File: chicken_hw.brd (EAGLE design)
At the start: 25.7 x 38.1 mm, 19 parts, among them U2 CD74HC4051PWR

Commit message: Fix ERC errors w/ V0.3 board  VCC and S2 not connected (unrouted)
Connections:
- removed net VCC: U2.16
- net 3.3V: now also U2.16
- net N$1: now also U2.9
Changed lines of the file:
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@@
 <wire x1="19.0618" y1="22.4926" x2="20.0152" y2="21.5392" width="0.254" layer="1"/>
 <wire x1="22.86" y1="13.97" x2="20.0152" y2="13.97" width="0.254" layer="1"/>
+<contactref element="U2" pad="16"/>
+<wire x1="17.2466" y1="22.4926" x2="10.5156" y2="26.4414" width="0" layer="19" extent="1-1"/>
 </signal>
 <signal name="EN_MUX">
@@
 <signal name="N$1">
 <contactref element="R1" pad="2"/>
+<contactref element="U2" pad="9"/>
+<wire x1="8.89" y1="16.1535" x2="15.0876" y2="26.4414" width="0" layer="19" extent="1-1"/>
 </signal>
 <signal name="N$8">
@@
 <wire x1="4.445" y1="24.13" x2="4.7752" y2="23.7998" width="0.254" layer="1"/>
 </signal>
-<signal name="VCC">
-<contactref element="U2" pad="16"/>
-</signal>
 <signal name="N$2">

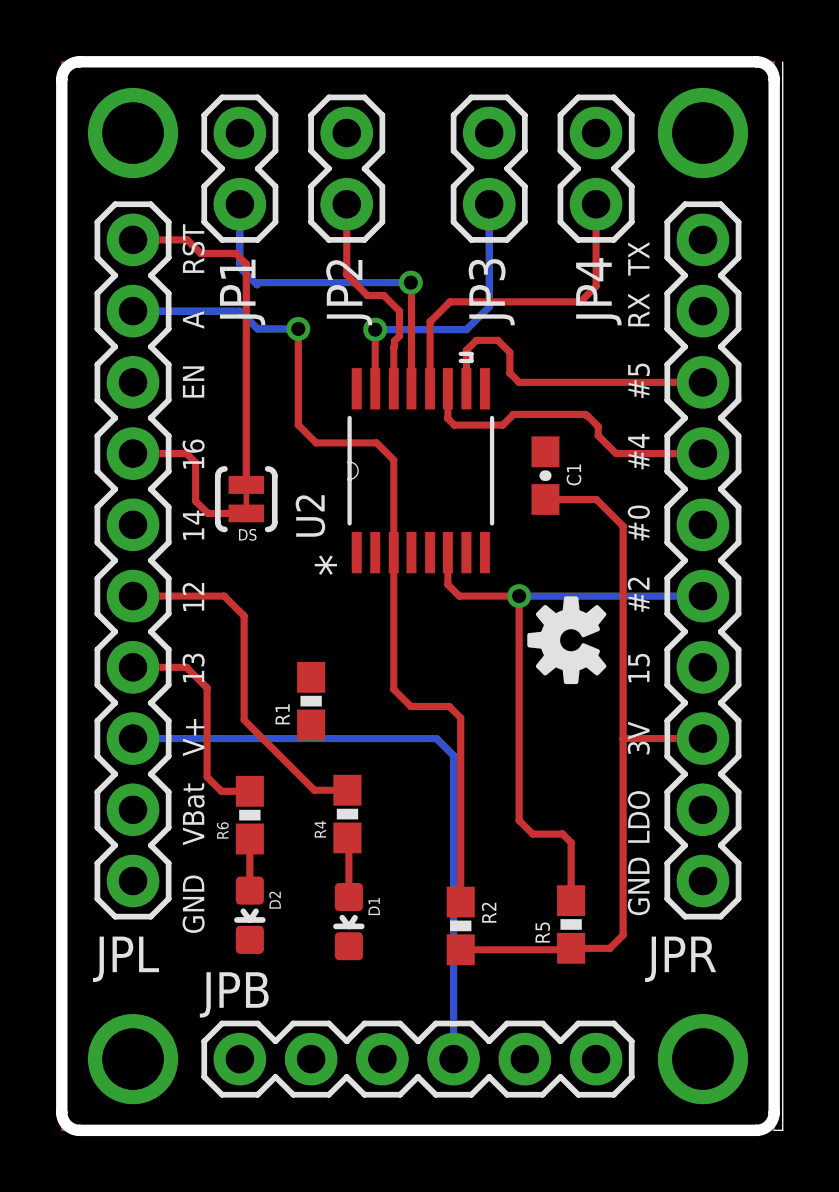
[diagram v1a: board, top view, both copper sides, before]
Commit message: Route missing signals for mux from 12c953b27b064bb54cf89404
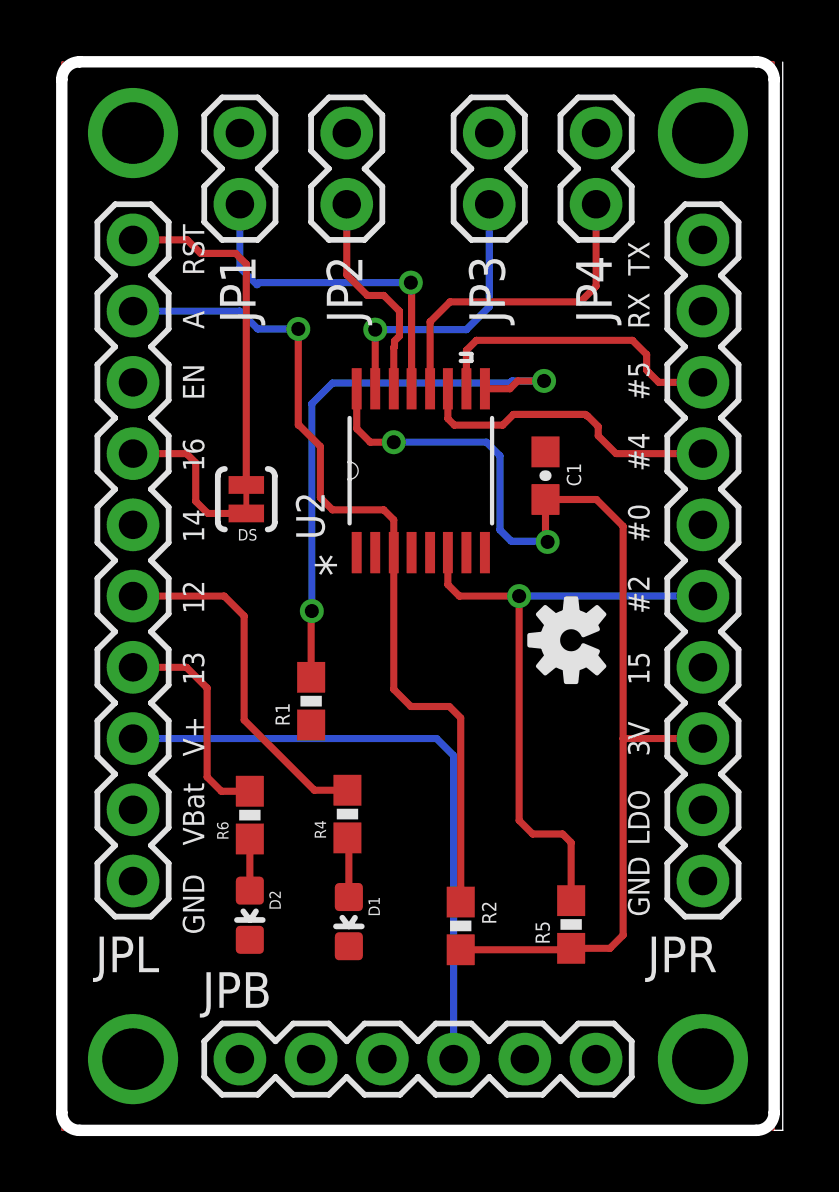
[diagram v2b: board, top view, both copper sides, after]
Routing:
- net N$1: track 0.00 -> 20.6 mm, vias 0 -> 2
- net 3.3V: track 26.6 -> 39.6 mm, vias 0 -> 2
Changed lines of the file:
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@@
 <contactref element="R2" pad="1"/>
 <contactref element="U2" pad="3"/>
-<wire x1="11.8364" y1="20.5994" x2="11.8364" y2="23.9014" width="0.254" layer="1"/>
-<wire x1="11.8364" y1="23.9014" x2="11.2268" y2="24.511" width="0.254" layer="1"/>
-<wire x1="11.2268" y1="24.511" x2="9.0678" y2="24.511" width="0.254" layer="1"/>
-<wire x1="9.0678" y1="24.511" x2="8.4328" y2="25.146" width="0.254" layer="1"/>
 <via x="8.4328" y="28.575" extent="1-16" drill="0.5" diameter="0.254"/>
 <wire x1="8.4328" y1="28.575" x2="8.4328" y2="25.146" width="0.254" layer="1"/>
@@
 <wire x1="11.8364" y1="20.5994" x2="11.8364" y2="15.7226" width="0.254" layer="1"/>
 <wire x1="11.8364" y1="15.7226" x2="12.446" y2="15.113" width="0.254" layer="1"/>
+<wire x1="8.4328" y1="25.146" x2="8.4582" y2="25.146" width="0.254" layer="1"/>
+<wire x1="8.4582" y1="25.146" x2="9.2202" y2="24.384" width="0.254" layer="1"/>
+<wire x1="9.2202" y1="24.384" x2="9.2202" y2="22.5552" width="0.254" layer="1"/>
+<wire x1="9.2202" y1="22.5552" x2="9.652" y2="22.1234" width="0.254" layer="1"/>
+<wire x1="9.652" y1="22.1234" x2="11.4808" y2="22.1234" width="0.254" layer="1"/>
+<wire x1="11.8364" y1="20.5994" x2="11.8364" y2="21.7678" width="0.254" layer="1"/>
+<wire x1="11.8364" y1="21.7678" x2="11.4808" y2="22.1234" width="0.254" layer="1"/>
 </signal>
 <signal name="EN">
@@
 <wire x1="14.4272" y1="26.4414" x2="14.4272" y2="27.813" width="0.254" layer="1"/>
 <wire x1="14.4272" y1="27.813" x2="14.7828" y2="28.1686" width="0.254" layer="1"/>
-<wire x1="14.7828" y1="28.1686" x2="15.5448" y2="28.1686" width="0.254" layer="1"/>
-<wire x1="15.5448" y1="28.1686" x2="15.9766" y2="27.7368" width="0.254" layer="1"/>
-<wire x1="22.86" y1="26.67" x2="16.3068" y2="26.67" width="0.254" layer="1"/>
-<wire x1="16.3068" y1="26.67" x2="15.9766" y2="27.0002" width="0.254" layer="1"/>
-<wire x1="15.9766" y1="27.0002" x2="15.9766" y2="27.7368" width="0.254" layer="1"/>
+<wire x1="14.7828" y1="28.1686" x2="20.3454" y2="28.1686" width="0.254" layer="1"/>
+<wire x1="20.3454" y1="28.1686" x2="20.8534" y2="27.6606" width="0.254" layer="1"/>
+<wire x1="20.8534" y1="27.6606" x2="20.8534" y2="27.1018" width="0.254" layer="1"/>
+<wire x1="20.8534" y1="27.1018" x2="20.9042" y2="27.051" width="0.254" layer="1"/>
+<wire x1="22.86" y1="26.67" x2="21.2852" y2="26.67" width="0.254" layer="1"/>
+<wire x1="21.2852" y1="26.67" x2="20.9042" y2="27.051" width="0.254" layer="1"/>
 </signal>
 <signal name="RX_R">
@@
 <wire x1="22.86" y1="13.97" x2="20.0152" y2="13.97" width="0.254" layer="1"/>
 <contactref element="U2" pad="16"/>
-<wire x1="17.2466" y1="22.4926" x2="10.5156" y2="26.4414" width="0" layer="19" extent="1-1"/>
+<wire x1="10.5156" y1="26.4414" x2="10.5156" y2="25.019" width="0.254" layer="1"/>
+<wire x1="10.5156" y1="25.019" x2="10.9982" y2="24.5364" width="0.254" layer="1"/>
+<via x="11.8364" y="24.5364" extent="1-16" drill="0.5"/>
+<via x="17.3228" y="20.9804" extent="1-16" drill="0.5"/>
+<wire x1="17.2466" y1="22.4926" x2="17.2466" y2="21.0566" width="0.254" layer="1"/>
+<wire x1="17.2466" y1="21.0566" x2="17.3228" y2="20.9804" width="0.254" layer="1"/>
+<wire x1="11.8364" y1="24.5364" x2="10.9982" y2="24.5364" width="0.254" layer="1"/>
+<wire x1="11.8364" y1="24.5364" x2="15.1384" y2="24.5364" width="0.254" layer="16"/>
+<wire x1="15.1384" y1="24.5364" x2="15.621" y2="24.0538" width="0.254" layer="16"/>
+<wire x1="15.621" y1="24.0538" x2="15.621" y2="21.4122" width="0.254" layer="16"/>
+<wire x1="15.621" y1="21.4122" x2="16.0274" y2="21.0058" width="0.254" layer="16"/>
+<wire x1="16.0274" y1="21.0058" x2="17.2974" y2="21.0058" width="0.254" layer="16"/>
+<wire x1="17.2974" y1="21.0058" x2="17.3228" y2="20.9804" width="0.254" layer="16"/>
 </signal>
 <signal name="EN_MUX">
@@
 <contactref element="R1" pad="2"/>
 <contactref element="U2" pad="9"/>
-<wire x1="8.89" y1="16.1535" x2="15.0876" y2="26.4414" width="0" layer="19" extent="1-1"/>
+<via x="8.9154" y="18.5166" extent="1-16" drill="0.5"/>
+<via x="17.1958" y="26.7208" extent="1-16" drill="0.5"/>
+<wire x1="8.89" y1="16.1535" x2="8.89" y2="18.4912" width="0.254" layer="1"/>
+<wire x1="8.89" y1="18.4912" x2="8.9154" y2="18.5166" width="0.254" layer="1"/>
+<wire x1="15.0876" y1="26.4414" x2="15.9766" y2="26.4414" width="0.254" layer="1"/>
+<wire x1="15.9766" y1="26.4414" x2="16.256" y2="26.7208" width="0.254" layer="1"/>
+<wire x1="16.256" y1="26.7208" x2="17.1958" y2="26.7208" width="0.254" layer="1"/>
+<wire x1="8.9154" y1="18.5166" x2="8.9154" y2="25.908" width="0.254" layer="16"/>
+<wire x1="8.9154" y1="25.908" x2="9.652" y2="26.6446" width="0.254" layer="16"/>
+<wire x1="9.652" y1="26.6446" x2="15.9766" y2="26.6446" width="0.254" layer="16"/>
+<wire x1="17.1958" y1="26.7208" x2="16.0528" y2="26.7208" width="0.254" layer="16"/>
+<wire x1="16.0528" y1="26.7208" x2="15.9766" y2="26.6446" width="0.254" layer="16"/>
 </signal>
 <signal name="N$8">

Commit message: Rev silkscreen to ver 0.4
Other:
- board text added: "4-input Temp Sensor jason.k.holden@gmail.com ver 0.4 1-3-2016"
- board text removed: "4-input Temp Sensor jason.k.holden@gmail.com ver 0.3 12-13-2015"
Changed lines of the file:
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@@
 <text x="12.6492" y="19.1516" size="1.016" layer="22" font="vector" ratio="12" rot="MR90" align="center">4-input Temp Sensor
 jason.k.holden@gmail.com
-ver 0.3 12-13-2015</text>
+ver 0.4 1-3-2016</text>
 </plain>
 <attributes>
